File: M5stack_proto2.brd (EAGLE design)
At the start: 50 x 50 mm, 2 parts, among them CN1 CON_PINHD-2X15, CN2 CON_PINHD-2X15

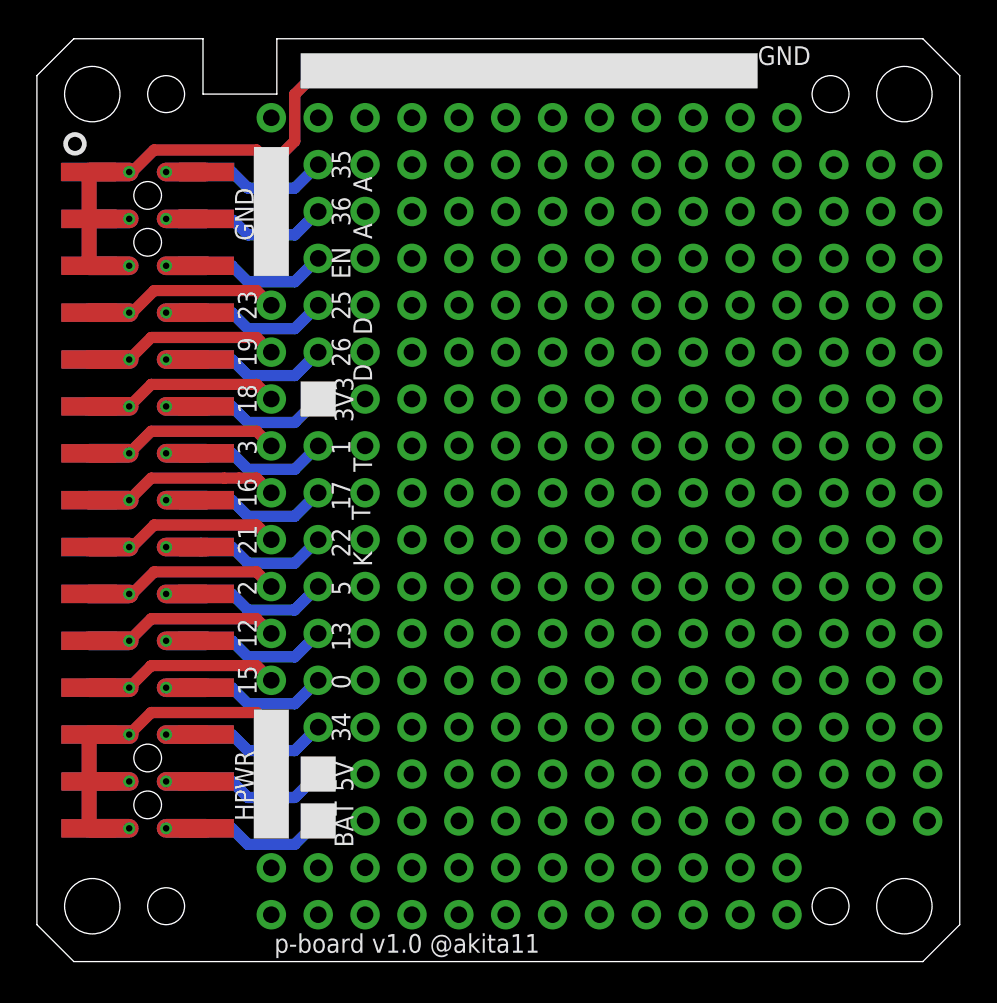
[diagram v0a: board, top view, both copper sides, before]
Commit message: シルク文字・コネクタ位置決め穴・コネクタパッドを調整
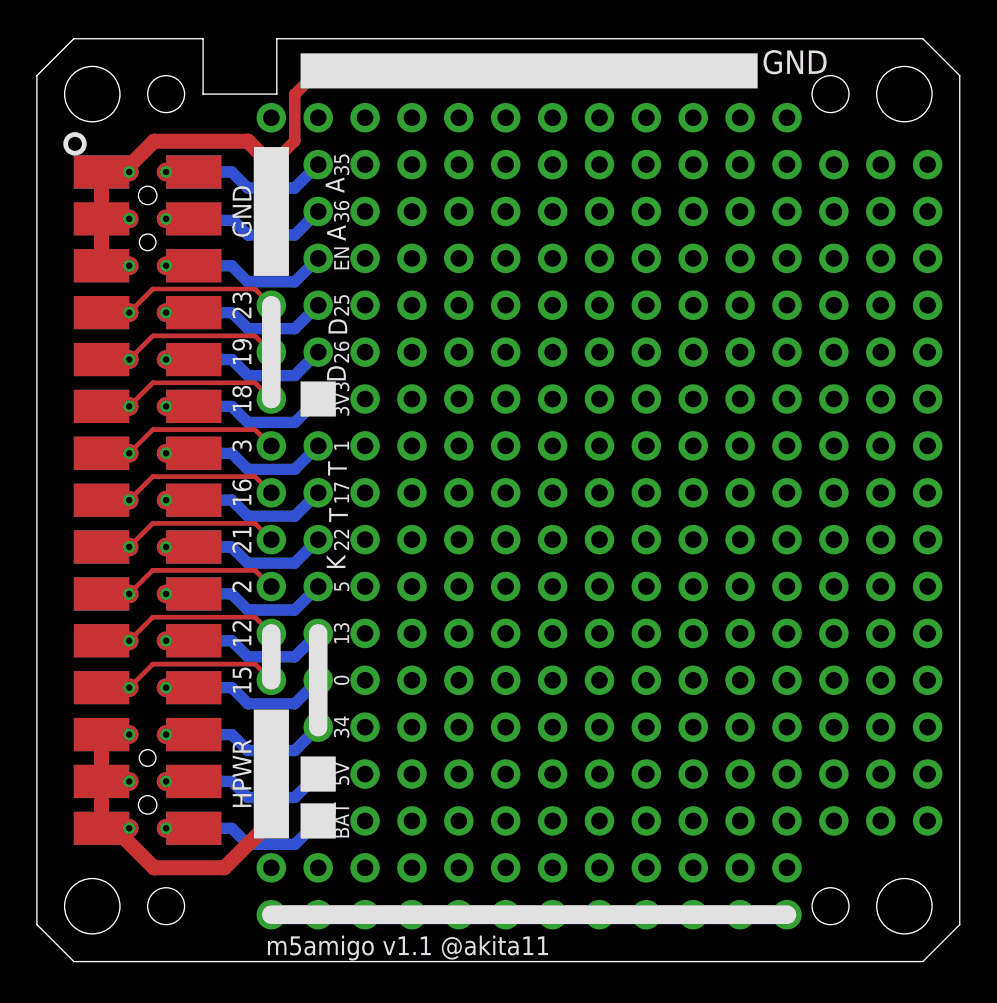
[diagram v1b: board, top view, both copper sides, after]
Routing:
- net N$19: track 0.00 -> 55.9 mm, vias 1 -> 2
- net 6: track 72.0 -> 69.3 mm
- net 30: track 36.8 -> 35.4 mm
- net 24: track 12.9 -> 11.6 mm
- net 16: track 12.9 -> 11.6 mm
- net 14: track 12.9 -> 11.6 mm
- net 12: track 12.9 -> 11.6 mm
- net 10: track 12.9 -> 11.6 mm
- net 8: track 12.9 -> 11.8 mm
- net 20: track 12.9 -> 11.8 mm
- net 18: track 12.9 -> 11.8 mm
- net 22: track 12.9 -> 11.9 mm
- net 3: track 11.3 -> 10.6 mm
- net 29: track 11.3 -> 10.6 mm
- net 27: track 11.3 -> 10.6 mm
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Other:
- board text added: "m5amigo v1.1 @akita11"
- board text removed: "p-board v1.0 @akita11"
